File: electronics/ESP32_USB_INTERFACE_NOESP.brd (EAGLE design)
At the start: 44.2 x 25.4 mm, 26 parts, among them J1 10118193-0001LF, T1 MMBT2222A, T2 MMBT2222A

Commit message: Update mainboard and progboard to use smaller connector
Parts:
- XPROG: value (none) -> PR20B04HBDN; device con-lstb:MA04-2 -> mccloud:PR20B04HBDN
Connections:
- net 3V3: now also XPROG.P$8; no longer XPROG.8
- net 5V: now also XPROG.P$6; no longer XPROG.6
- net GND: now also XPROG.P$2; no longer XPROG.2
- net IO0: now also XPROG.P$3; no longer XPROG.3
- net RST: now also XPROG.P$1; no longer XPROG.1
- net RX: now also XPROG.P$7; no longer XPROG.7
- net TX: now also XPROG.P$5; no longer XPROG.5
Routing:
- net IO0: track 16.1 -> 17.9 mm
- net 3V3: track 67.8 -> 69.4 mm
- net RX: track 30.8 -> 32.3 mm
- net RST: track 15.3 -> 16.7 mm
- net TX: track 29.2 -> 28.6 mm, vias 0 -> 1
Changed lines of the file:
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@@
 <attribute name="VALUE" x="55.88" y="37.973" size="1.27" layer="27" ratio="10"/>
 </element>
-<element name="XPROG" library="con-lstb" library_urn="urn:adsk.eagle:library:162" package="MA04-2" package3d_urn="urn:adsk.eagle:package:8368/1" value="" x="55.88" y="50.546" smashed="yes">
-<attribute name="MF" value="" x="74.93" y="34.036" size="1.778" layer="27" display="off"/>
-<attribute name="MPN" value="" x="74.93" y="34.036" size="1.778" layer="27" display="off"/>
+<element name="XPROG" library="mccloud" package="PR20B04HBDN" value="PR20B04HBDN" x="55.88" y="50.546" smashed="yes">
 <attribute name="NAME" x="61.341" y="52.578" size="0.8128" layer="25" font="vector" ratio="15" rot="R270"/>
-<attribute name="OC_FARNELL" value="unknown" x="74.93" y="34.036" size="1.778" layer="27" display="off"/>
-<attribute name="OC_NEWARK" value="unknown" x="74.93" y="34.036" size="1.778" layer="27" display="off"/>
-<attribute name="POPULARITY" value="11" x="74.93" y="34.036" size="1.778" layer="27" display="off"/>
 <attribute name="VALUE" x="55.88" y="46.355" size="1.27" layer="27" ratio="10"/>
 </element>
@@
 </signal>
 <signal name="3V3">
-<contactref element="XPROG" pad="8"/>
+<contactref element="XPROG" pad="P$8"/>
 <contactref element="JP1" pad="1"/>
 <contactref element="JP2" pad="1"/>
@@
 <contactref element="C2" pad="2"/>
 <contactref element="C3" pad="1"/>
-<wire x1="59.69" y1="51.816" x2="61.976" y2="49.53" width="1.016" layer="1"/>
-<wire x1="61.976" y1="49.53" x2="61.976" y2="38.608" width="1.016" layer="1"/>
+<wire x1="61.976" y1="38.608" x2="61.976" y2="49.53" width="1.016" layer="1"/>
 <wire x1="22.352" y1="44.45" x2="22.352" y2="41.148" width="1.016" layer="1"/>
 <wire x1="22.352" y1="41.148" x2="22.352" y2="37.846" width="1.016" layer="1"/>
@@
 <wire x1="61.976" y1="38.608" x2="60.198" y2="36.83" width="1.016" layer="1"/>
 <wire x1="60.198" y1="36.83" x2="36.576" y2="36.83" width="1.016" layer="1"/>
+<wire x1="61.976" y1="49.53" x2="60.325" y2="51.181" width="0.9906" layer="1"/>
+<wire x1="60.325" y1="51.181" x2="57.785" y2="51.181" width="0.9906" layer="1"/>
 </signal>
 <signal name="IO0">
 <contactref element="T2" pad="C"/>
-<contactref element="XPROG" pad="3"/>
+<contactref element="XPROG" pad="P$3"/>
 <contactref element="XDEBG" pad="4"/>
-<wire x1="54.61" y1="49.276" x2="54.61" y2="43.434" width="0.381" layer="16"/>
-<wire x1="48.598" y1="47.752" x2="53.086" y2="47.752" width="0.508" layer="1"/>
-<wire x1="53.086" y1="47.752" x2="54.61" y2="49.276" width="0.508" layer="1"/>
 <contactref element="PROG" pad="P$3"/>
 <contactref element="PROG" pad="P$4"/>
 <wire x1="48.679" y1="51.344" x2="48.679" y2="47.833" width="0.508" layer="1"/>
 <wire x1="48.679" y1="47.833" x2="48.598" y2="47.752" width="0.508" layer="1"/>
+<wire x1="54.61" y1="43.434" x2="54.61" y2="49.276" width="0.254" layer="16"/>
+<wire x1="54.61" y1="49.276" x2="55.245" y2="49.911" width="0.254" layer="16"/>
+<wire x1="54.8814" y1="49.53555625" x2="54.8814" y2="49.5474" width="0.508" layer="1"/>
+<wire x1="54.8814" y1="49.5474" x2="55.245" y2="49.911" width="0.508" layer="1"/>
+<wire x1="48.598" y1="47.752" x2="53.09784375" y2="47.752" width="0.508" layer="1"/>
+<wire x1="53.09784375" y1="47.752" x2="54.8814" y2="49.53555625" width="0.508" layer="1"/>
 <wire x1="40.729" y1="51.344" x2="48.679" y2="51.344" width="0" layer="19" extent="1-1"/>
 </signal>
@@
 <contactref element="RESET" pad="P$3"/>
 <contactref element="RESET" pad="P$4"/>
-<contactref element="XPROG" pad="1"/>
+<contactref element="XPROG" pad="P$1"/>
 <contactref element="XDEBG" pad="2"/>
-<wire x1="52.07" y1="49.276" x2="52.07" y2="43.434" width="0.508" layer="16"/>
 <wire x1="48.598" y1="42.926" x2="51.562" y2="42.926" width="0.508" layer="1"/>
 <wire x1="51.562" y1="42.926" x2="52.07" y2="43.434" width="0.508" layer="1"/>
@@
 <wire x1="48.171" y1="41.059" x2="48.171" y2="39.334" width="0.508" layer="1"/>
 <wire x1="48.598" y1="41.486" x2="48.171" y2="41.059" width="0.508" layer="1"/>
+<wire x1="52.07" y1="43.434" x2="53.975" y2="45.339" width="0.254" layer="16"/>
+<wire x1="53.975" y1="45.339" x2="53.975" y2="49.911" width="0.254" layer="16"/>
 <wire x1="40.221" y1="39.334" x2="48.171" y2="39.334" width="0" layer="19" extent="1-1"/>
 </signal>
 <signal name="RX">
 <contactref element="U$1" pad="20"/>
-<contactref element="XPROG" pad="7"/>
+<contactref element="XPROG" pad="P$7"/>
 <contactref element="XDEBG" pad="8"/>
-<wire x1="59.69" y1="49.276" x2="59.69" y2="43.434" width="0.381" layer="16"/>
 <wire x1="59.69" y1="43.434" x2="58.154" y2="44.97" width="0.254" layer="1"/>
 <wire x1="38.1787375" y1="43.446" x2="35.986" y2="43.446" width="0.254" layer="1"/>
 <wire x1="58.154" y1="44.97" x2="39.7027375" y2="44.97" width="0.254" layer="1"/>
 <wire x1="39.7027375" y1="44.97" x2="38.1787375" y2="43.446" width="0.254" layer="1"/>
+<wire x1="57.7596" y1="46.75555" x2="57.785" y2="46.78095" width="0.254" layer="16"/>
+<wire x1="57.785" y1="46.78095" x2="57.785" y2="49.911" width="0.254" layer="16"/>
+<wire x1="59.69" y1="43.434" x2="57.7596" y2="45.3644" width="0.254" layer="16"/>
+<wire x1="57.7596" y1="45.3644" x2="57.7596" y2="46.75555" width="0.254" layer="16"/>
 </signal>
 <signal name="TX">
 <contactref element="U$1" pad="21"/>
-<contactref element="XPROG" pad="5"/>
+<contactref element="XPROG" pad="P$5"/>
 <contactref element="XDEBG" pad="6"/>
-<wire x1="57.15" y1="49.276" x2="57.15" y2="43.434" width="0.381" layer="16"/>
-<wire x1="53.344" y1="45.47" x2="39.628" y2="45.47" width="0.254" layer="1"/>
-<wire x1="53.344" y1="45.47" x2="57.15" y2="49.276" width="0.254" layer="1"/>
 <wire x1="38.104" y1="43.946" x2="35.986" y2="43.946" width="0.254" layer="1"/>
-<wire x1="39.628" y1="45.47" x2="38.104" y2="43.946" width="0.254" layer="1"/>
+<wire x1="38.104" y1="43.946" x2="39.628" y2="45.47" width="0.254" layer="1"/>
+<wire x1="57.15" y1="43.434" x2="57.15" y2="45.72" width="0.254" layer="16"/>
+<wire x1="57.15" y1="45.72" x2="57.15" y2="49.276" width="0.254" layer="16"/>
+<wire x1="57.15" y1="49.276" x2="56.515" y2="49.911" width="0.254" layer="16"/>
+<wire x1="56.3034375" y1="45.47" x2="56.3848375" y2="45.5514" width="0.254" layer="1"/>
+<via x="56.3848375" y="45.5514" extent="1-16" drill="0.35"/>
+<wire x1="56.3848375" y1="45.5514" x2="56.9814" y2="45.5514" width="0.254" layer="16"/>
+<wire x1="56.9814" y1="45.5514" x2="57.15" y2="45.72" width="0.254" layer="16"/>
+<wire x1="39.628" y1="45.47" x2="56.3034375" y2="45.47" width="0.254" layer="1"/>
 </signal>
 <signal name="RTS">
@@
 </signal>
 <signal name="GND">
-<contactref element="XPROG" pad="2"/>
+<contactref element="XPROG" pad="P$2"/>
 <contactref element="XDEBG" pad="1"/>
 <contactref element="C1" pad="2"/>
@@
 <via x="50.8" y="38.354" extent="1-16" drill="0.508"/>
 <via x="58.42" y="46.482" extent="1-16" drill="0.508"/>
-<via x="55.88" y="46.228" extent="1-16" drill="0.508"/>
+<via x="55.626" y="47.752" extent="1-16" drill="0.508"/>
 </signal>
 <signal name="5V">
-<contactref element="XPROG" pad="6"/>
+<contactref element="XPROG" pad="P$6"/>
 <contactref element="R5" pad="1"/>
-<wire x1="55.46" y1="53.506" x2="39.536" y2="53.506" width="1.016" layer="1"/>
-<wire x1="55.46" y1="53.506" x2="57.15" y2="51.816" width="1.016" layer="1"/>
+<wire x1="39.536" y1="53.506" x2="55.46" y2="53.506" width="1.016" layer="1"/>
 <wire x1="39.536" y1="53.506" x2="38.608" y2="52.578" width="0.635" layer="1"/>
 <wire x1="38.608" y1="52.578" x2="38.608" y2="52.07" width="0.635" layer="1"/>
@@
 <wire x1="34.544" y1="52.07" x2="32.512" y2="52.07" width="0.635" layer="1"/>
 <wire x1="32.512" y1="52.07" x2="30.48" y2="50.038" width="0.635" layer="1"/>
+<wire x1="55.46" y1="53.506" x2="56.515" y2="52.451" width="0.9906" layer="1"/>
+<wire x1="56.515" y1="52.451" x2="56.515" y2="51.181" width="0.9906" layer="1"/>
 </signal>
 <signal name="N$5">

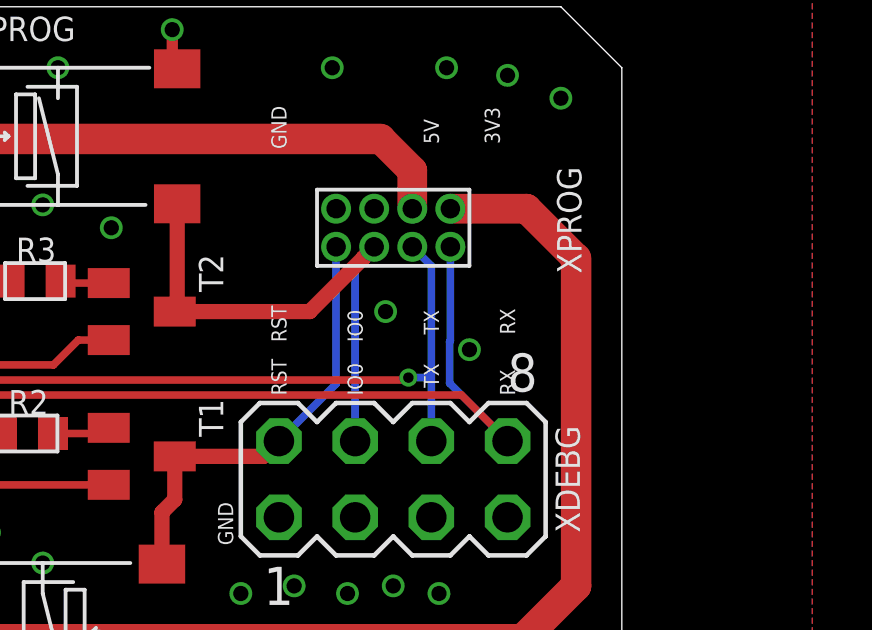
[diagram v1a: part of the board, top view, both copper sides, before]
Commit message: Various connector changes and other miscellany
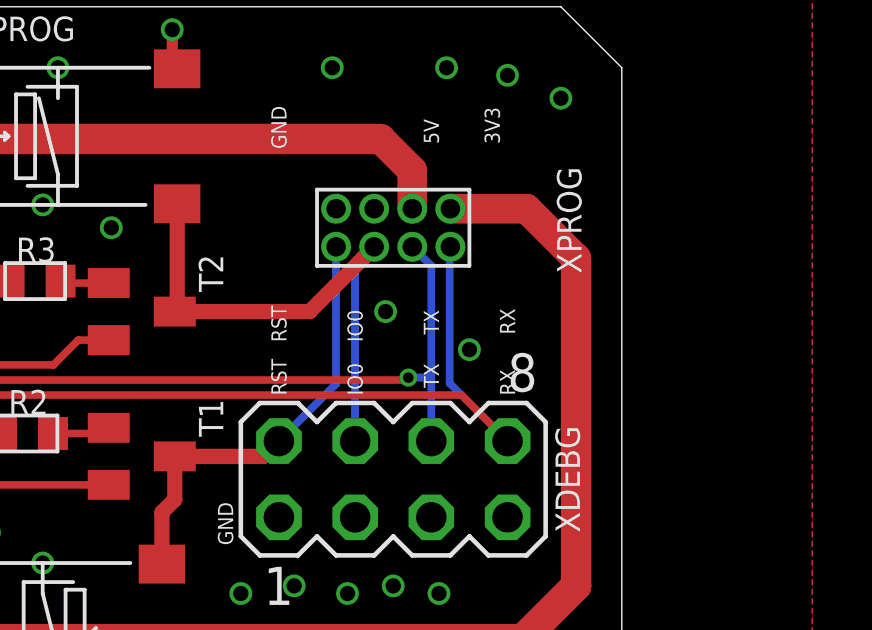
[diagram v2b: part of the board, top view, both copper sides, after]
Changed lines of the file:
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@@
 <layers>
 <layer number="1" name="Top" color="4" fill="1" visible="yes" active="yes"/>
-<layer number="2" name="Route2" color="16" fill="1" visible="no" active="yes"/>
+<layer number="2" name="Route2" color="16" fill="1" visible="yes" active="yes"/>
 <layer number="3" name="Route3" color="17" fill="1" visible="no" active="no"/>
 <layer number="4" name="Route4" color="18" fill="1" visible="no" active="no"/>
@@
 <layer number="25" name="tNames" color="7" fill="1" visible="yes" active="yes"/>
 <layer number="26" name="bNames" color="7" fill="1" visible="no" active="yes"/>
-<layer number="27" name="tValues" color="7" fill="1" visible="no" active="yes"/>
+<layer number="27" name="tValues" color="7" fill="1" visible="yes" active="yes"/>
 <layer number="28" name="bValues" color="7" fill="1" visible="no" active="yes"/>
 <layer number="29" name="tStop" color="7" fill="3" visible="no" active="yes"/>
@@
 </element>
 <element name="C4" library="mccloud" package="C0603" value="1uF" x="37.465" y="39.37" smashed="yes" rot="R180">
+<attribute name="COMPONENT" value="CL10A105KB8NNNC" x="37.465" y="39.37" size="1.778" layer="27" rot="R180" display="off"/>
 <attribute name="NAME" x="38.1" y="38.227" size="0.8128" layer="25" font="vector" ratio="15" rot="R180"/>
 <attribute name="VALUE" x="38.1" y="41.275" size="0.8128" layer="27" font="vector" ratio="15" rot="R180"/>
@@
 </element>
 <element name="R4" library="mccloud" package="R0603" value="1M" x="32.004" y="55.118" smashed="yes" rot="R90">
+<attribute name="COMPONENT" value="CR0603-JW-105ELF" x="32.004" y="55.118" size="1.778" layer="27" rot="R90" display="off"/>
 <attribute name="NAME" x="31.369" y="54.483" size="0.8128" layer="25" font="vector" ratio="15" rot="R90"/>
 <attribute name="POPULARITY" value="77" x="75.184" y="70.358" size="1.778" layer="27" rot="R90" display="off"/>
@@
 <wire x1="58.154" y1="44.97" x2="39.7027375" y2="44.97" width="0.254" layer="1"/>
 <wire x1="39.7027375" y1="44.97" x2="38.1787375" y2="43.446" width="0.254" layer="1"/>
-<wire x1="57.7596" y1="46.75555" x2="57.785" y2="46.78095" width="0.254" layer="16"/>
-<wire x1="57.785" y1="46.78095" x2="57.785" y2="49.911" width="0.254" layer="16"/>
+<wire x1="57.7596" y1="49.8856" x2="57.785" y2="49.911" width="0.254" layer="16"/>
+<wire x1="57.7596" y1="49.8856" x2="57.7596" y2="45.3644" width="0.254" layer="16"/>
 <wire x1="59.69" y1="43.434" x2="57.7596" y2="45.3644" width="0.254" layer="16"/>
-<wire x1="57.7596" y1="45.3644" x2="57.7596" y2="46.75555" width="0.254" layer="16"/>
 </signal>
 <signal name="TX">
